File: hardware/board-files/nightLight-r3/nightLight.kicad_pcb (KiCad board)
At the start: 2 copper layers, 85 x 85 mm, 41 parts, among them IC1 PAM2401SCADJ, IC2 MCP73123T-22SI_MF, J1 USB_C_Receptacle_PowerOnly_6P, J2 Conn_01x03, J3 Conn_01x03, J4 Conn_01x03, J5 Conn_01x03, J6 Conn_01x05_Pin, SW1 TILT, U2 ATtiny1614-SS

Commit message: finished shematic and added to PCB
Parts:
- removed BT1: Battery_Cell, myFootprintDesigns:14500 Holder
- removed C7: 0.1uF, Capacitor_SMD:C_0805_2012Metric
- removed IC2: MCP73123T-22SI_MF, MCP73123T-22SI_MF:SON50P300X300X100-11N-D
- removed J6: Conn_01x05_Pin, Connector_PinSocket_2.54mm:PinSocket_1x05_P2.54mm_Vertical_SMD_Pin1Left
- removed LED1: IN-S124ARUW, KiCad-SMTLED:INS124ARUW
- removed R12: 10k, Resistor_SMD:R_0805_2012Metric
- removed R13: 1M, Resistor_SMD:R_0805_2012Metric
- removed S1: PTS526_SM08_SMTR2_LFS, PTS526_SM08_SMTR2_LFS:SW_PTS526_SM08_SMTR2_LFS
- removed U2: ATtiny1614-SS, Package_SO:SOIC-14_3.9x8.7mm_P1.27mm
- added BT2: Battery_Cell, myFootprintDesigns:14500 Holder, F.Cu at (66.0, 93.4)
- added C3: 22uF, Capacitor_SMD:C_0805_2012Metric, F.Cu at (39.2, 120.9)
- added C8: 4.7uF, Capacitor_SMD:C_0805_2012Metric, F.Cu at (61.6, 108.1)
- added D3: BAT54C, BAT54C:SOT23-R, F.Cu at (40.0, 116.6)
- added IC3: MCP73123T-22SI_MF, MCP73123T-22SI_MF:SON50P300X300X100-11N-D, F.Cu at (62.0, 104.3)
- added J7: USB_C_Receptacle_PowerOnly_6P, myFootprintDesigns:USB-C_PWR, F.Cu at (41.0, 108.2)
- added LED2: IN-S124ARUW, KiCad-SMTLED:INS124ARUW, F.Cu at (56.6, 105.6)
- added Q1: NMOS, IRLML6402TRPBF:SOT95P237X112-3N, F.Cu at (35.4, 117.1)
- added Q2: PMOS, IRLML6344TRPBF:SOT95P240X112-3N, F.Cu at (34.7, 121.5)
- added R1: 750K, Resistor_SMD:R_0805_2012Metric, F.Cu at (39.1, 123.9)
- added R14: 5.1k, Resistor_SMD:R_0805_2012Metric, F.Cu at (51.7, 103.4)
- added R15: 1K, Resistor_SMD:R_0805_2012Metric, F.Cu at (51.7, 106.4)
- added R16: 5.1K, Resistor_SMD:R_0805_2012Metric, F.Cu at (51.7, 109.3)
- added U1: ATtiny1614-SS, Package_SO:SOIC-14_3.9x8.7mm_P1.27mm, F.Cu at (48.3, 120.0)
- C2: value 4.7uF -> 0.1uF
- C4: value 4.7uF -> 22uF
- C5: value 22uF -> 4.7uF
- C6: value 22uF -> 0.1uF
- J1: value USB_C_Receptacle_PowerOnly_6P -> Conn_01x03; footprint myFootprintDesigns:USB-C_PWR -> Connector_PinHeader_2.54mm:PinHeader_1x03_P2.54mm_Vertical_SMD_Pin1Left
- J4: footprint Connector_PinHeader_2.54mm:PinHeader_1x03_P2.54mm_Vertical_SMD_Pin1Left -> myFootprintDesigns:spares_1*3
- J5: value Conn_01x03 -> Conn_01x05_Pin; footprint myFootprintDesigns:spares_1*3 -> Connector_PinSocket_2.54mm:PinSocket_1x05_P2.54mm_Vertical_SMD_Pin1Left
- R10: value 0 -> 10k
- R11: value 10k -> 1M
- R2: value 5.1k -> 1M
- R4: value 5.1k -> 10K
- R5: value 5.1K -> 1M
- R6: value 1K -> 0
- R7: value 750K -> 100K
- R8: value 100K -> 5.1k
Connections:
- B1 pad 1: Return -> /MCU/RETURN
- C1 pad 1: VBATT -> Net-(IC1-VIN)
- C2 pad 1: Net-(IC2-VDD_1) -> Net-(Q1-G)
- C4 pad 1: VBATT -> +5V
- C5 pad 1: +5V -> /Charge Controller/Vbus
- IC1 pad 3: VBATT -> Net-(IC1-VIN)
- J2 pad 2: LED_DATA -> Net-(J2-Pin_2)
- J3 pad 2: Net-(J3-Pin_2) -> Net-(J2-Pin_2)
- J4 pad 1: +5V -> /MCU/PA_1
- J4 pad 2: Net-(J3-Pin_2) -> /MCU/PA_2
- J4 pad 3: GND -> /MCU/PA_3
- J5 pad 1: PA_1 -> GND
- J5 pad 2: PA_2 -> /MCU/TX
- J5 pad 3: PA_3 -> /MCU/RX
- L1 pad 1: VBATT -> Net-(IC1-VIN)
- R10 pad 1: Batt_M -> +5V
- R10 pad 2: GND -> /MCU/TILT_SW
- R11 pad 1: +5V -> /MCU/SEND
- R11 pad 2: RST_SW -> /MCU/RETURN
- R2 pad 1: Net-(J1-CC2) -> /Charge Controller/Vbatt
- R2 pad 2: GND -> Net-(Q1-D)
- R3 pad 1: VBATT -> Net-(IC1-FB)
- R3 pad 2: Net-(IC1-EN) -> +5V
- R4 pad 1: Net-(J1-CC1) -> Net-(Q1-G)
- R4 pad 2: GND -> Net-(D3-Pad3)
- R5 pad 1: Net-(IC2-PROG) -> Net-(Q1-G)
- R6 pad 1: Net-(LED1-K) -> /Charge Controller/Vbatt
- R6 pad 2: Net-(IC2-STAT) -> /MCU/BATT_M
- R7 pad 1: Net-(IC1-FB) -> GND
- R7 pad 2: +5V -> Net-(IC1-FB)
- R8 pad 1: GND -> Net-(J7-CC2)
- R8 pad 2: Net-(IC1-FB) -> GND
- R9 pad 1: VBATT -> /MCU/BATT_M
- R9 pad 2: Batt_M -> GND
- SW1 pad 1: Tilt_SW -> /MCU/TILT_SW
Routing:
- net (no net): track 0.00 -> 85.0 mm
- net Net-(Q1-G): track 0.00 -> 73.0 mm
- net /Charge Controller/Vbatt: track 0.00 -> 58.8 mm
- net Net-(IC2-VDD_1): track 58.4 -> 0.00 mm
- net Net-(LED1-K): track 50.8 -> 0.00 mm
- net /MCU/RETURN: track 0.00 -> 36.8 mm
- net VBATT: track 20.3 -> 0.00 mm
- net RX: track 19.8 -> 0.00 mm
- net Return: track 18.7 -> 0.00 mm
- net RST_SW: track 18.1 -> 0.00 mm
- net Batt_M: track 17.6 -> 0.00 mm, vias 2 -> 0
- net Net-(J1-CC1): track 14.6 -> 0.00 mm
- net TX: track 14.4 -> 0.00 mm
- net Tilt_SW: track 9.29 -> 0.00 mm
- net /MCU/TILT_SW: track 0.00 -> 9.29 mm
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- added copper zone on F.Cu, net Net-(IC1-VIN)
- added copper zone on F.Cu, net Net-(Q1-G)
- removed copper zone on F.Cu, net Net-(IC2-PROG)
- removed copper zone on F.Cu, net Net-(IC2-VDD_1)
- removed copper zone on F.Cu, net VBATT

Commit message: first layout revision
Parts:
- removed BT2: Battery_Cell, myFootprintDesigns:14500 Holder
- removed C8: 4.7uF, Capacitor_SMD:C_0805_2012Metric
- removed D3: BAT54C, BAT54C:SOT23-R
- removed IC3: MCP73123T-22SI_MF, MCP73123T-22SI_MF:SON50P300X300X100-11N-D
- removed J7: USB_C_Receptacle_PowerOnly_6P, myFootprintDesigns:USB-C_PWR
- removed LED2: IN-S124ARUW, KiCad-SMTLED:INS124ARUW
- removed R15: 1K, Resistor_SMD:R_0805_2012Metric
- removed R16: 5.1K, Resistor_SMD:R_0805_2012Metric
- removed U9: ~, myFootprintDesigns:fireflyTouchNB
- added BT1: Battery_Cell, myFootprintDesigns:14500 Holder, F.Cu at (150.0, 100.0)
- added C7: 0.1uF, Capacitor_SMD:C_0805_2012Metric, F.Cu at (151.9, 84.0)
- added D1: BAT54C, BAT54C:SOT23-R, F.Cu at (184.2, 89.5)
- added IC2: MCP73123T-22SI_MF, MCP73123T-22SI_MF:SON50P300X300X100-11N-D, F.Cu at (177.2, 110.5)
- added J6: Conn_01x03, Connector_PinHeader_2.54mm:PinHeader_1x03_P2.54mm_Vertical_SMD_Pin1Left, F.Cu at (167.0, 115.0)
- added LED1: IN-S124ARUW, KiCad-SMTLED:INS124ARUW, F.Cu at (139.0, 131.0)
- added R12: 1M, Resistor_SMD:R_0805_2012Metric, F.Cu at (162.5, 80.0)
- added R13: 10k, Resistor_SMD:R_0805_2012Metric, F.Cu at (126.0, 78.0)
- added U2: ~, myFootprintDesigns:fireflyTouchNB, B.Cu at (132.0, 122.5)
- C1: value 22uF -> 0.1uF
- C2, C6: value 0.1uF -> 22uF
- C4: value 22uF -> 4.7uF
- J1: value Conn_01x03 -> USB_C_Receptacle_PowerOnly_6P; footprint Connector_PinHeader_2.54mm:PinHeader_1x03_P2.54mm_Vertical_SMD_Pin1Left -> myFootprintDesigns:USB-C_PWR
- J2: value Conn_01x03 -> Conn_01x05_Pin; footprint Connector_PinHeader_2.54mm:PinHeader_1x03_P2.54mm_Vertical_SMD_Pin1Left -> Connector_PinSocket_2.54mm:PinSocket_1x05_P2.54mm_Vertical_SMD_Pin1Left
- J3: footprint Connector_PinHeader_2.54mm:PinHeader_1x03_P2.54mm_Vertical_SMD_Pin1Left -> myFootprintDesigns:spares_1*3
- J4: footprint myFootprintDesigns:spares_1*3 -> Connector_PinHeader_2.54mm:PinHeader_1x03_P2.54mm_Vertical_SMD_Pin1Left
- J5: value Conn_01x05_Pin -> Conn_01x03; footprint Connector_PinSocket_2.54mm:PinSocket_1x05_P2.54mm_Vertical_SMD_Pin1Left -> Connector_PinHeader_2.54mm:PinHeader_1x03_P2.54mm_Vertical_SMD_Pin1Left
- R1: value 750K -> 10K
- R10: value 10k -> 5.1k
- R14: value 5.1k -> 1M
- R3: value 750K -> 1M
- R4: value 10K -> 750K
- R5: value 1M -> 750K
- R6: value 0 -> 100K
- R7: value 100K -> 1K
- R8: value 5.1k -> 5.1K
- R9: value 0 -> 5.1k
- U1: value ATtiny1614-SS -> ~; footprint Package_SO:SOIC-14_3.9x8.7mm_P1.27mm -> myFootprintDesigns:fireflyTouchNB; moved to B.Cu
- U8: value ~ -> ATtiny1614-SS; footprint myFootprintDesigns:fireflyTouchNB -> Package_SO:SOIC-14_3.9x8.7mm_P1.27mm; moved to F.Cu
- moved Q1 151.3 mm to (185.2, 96.5), turned to 180 degrees
- moved R1 150.5 mm to (186.2, 92.2), turned to 90 degrees
- moved Q2 149.8 mm to (182.0, 94.5), turned to -90 degrees
- moved C3 145.0 mm to (178.9, 82.5), turned to 180 degrees
- moved U1 123.8 mm to (172.1, 123.5), turned to 75 degrees
- moved R14 110.8 mm to (160.0, 80.0), turned to 90 degrees
- moved U8 50.5 mm to (144.0, 81.5), turned to 180 degrees
- moved R9 45.3 mm to (157.5, 125.0)
- moved R10 45.0 mm to (161.0, 125.0), turned to -90 degrees
- moved J4 44.8 mm to (144.0, 73.0), turned to -90 degrees
- moved R4 43.1 mm to (178.9, 85.8), turned to 180 degrees
- moved J3 42.5 mm to (135.3, 86.7), turned to 0 degrees
- moved R2 36.4 mm to (184.2, 100.2), turned to 90 degrees
- moved R8 33.5 mm to (176.8, 113.7), turned to 0 degrees
- moved R5 30.7 mm to (168.6, 84.1), turned to -90 degrees
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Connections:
- C1 pad 1: Net-(IC1-VIN) -> Net-(Q1-G)
- C2 pad 1: Net-(Q1-G) -> +5V
- C3 pad 1: +5V -> Net-(IC1-VIN)
- C4 pad 1: +5V -> /Charge Controller/Vbus
- C5 pad 1: /Charge Controller/Vbus -> /Charge Controller/Vbatt
- J2 pad 1: +5V -> GND
- J2 pad 2: Net-(J2-Pin_2) -> /MCU/TX
- J2 pad 3: GND -> /MCU/RX
- J3 pad 1: +5V -> /MCU/PA_1
- J3 pad 2: Net-(J2-Pin_2) -> /MCU/PA_2
- J3 pad 3: GND -> /MCU/PA_3
- J4 pad 1: /MCU/PA_1 -> +5V
- J4 pad 2: /MCU/PA_2 -> /MCU/LED_DATA
- J4 pad 3: /MCU/PA_3 -> GND
- J5 pad 1: GND -> +5V
- J5 pad 2: /MCU/TX -> Net-(J5-Pin_2)
- J5 pad 3: /MCU/RX -> GND
- R1 pad 1: Net-(IC1-VIN) -> Net-(Q1-G)
- R1 pad 2: Net-(IC1-EN) -> Net-(D1-Pad3)
- R10 pad 1: +5V -> Net-(J1-CC1)
- R10 pad 2: /MCU/TILT_SW -> GND
- R14 pad 1: Net-(J7-CC1) -> /MCU/BATT_M
- R3 pad 1: Net-(IC1-FB) -> Net-(Q1-G)
- R3 pad 2: +5V -> GND
- R4 pad 1: Net-(Q1-G) -> Net-(IC1-VIN)
- R4 pad 2: Net-(D3-Pad3) -> Net-(IC1-EN)
- R5 pad 1: Net-(Q1-G) -> Net-(IC1-FB)
- R5 pad 2: GND -> +5V
- R6 pad 1: /Charge Controller/Vbatt -> GND
- R6 pad 2: /MCU/BATT_M -> Net-(IC1-FB)
- R7 pad 1: GND -> Net-(LED1-K)
- R7 pad 2: Net-(IC1-FB) -> Net-(IC2-STAT)
- R9 pad 1: /MCU/BATT_M -> Net-(J1-CC2)
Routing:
- net /Charge Controller/Vbus: track 0.00 -> 94.7 mm
- net (no net): track 85.0 -> 0.00 mm
- net Net-(Q1-G): track 73.0 -> 13.1 mm
- net Net-(LED1-K): track 0.00 -> 50.8 mm
- net /MCU/FET_CONTROL: track 0.00 -> 47.5 mm, vias 0 -> 2
- net Net-(J5-Pin_2): track 0.00 -> 38.4 mm
- net Net-(J3-Pin_2): track 38.4 -> 0.00 mm
- net /MCU/RX: track 0.00 -> 19.8 mm
- net /MCU/RETURN: track 36.8 -> 18.7 mm
- net /MCU/BATT_M: track 1.86 -> 17.6 mm, vias 0 -> 2
- net /Charge Controller/Vbatt: track 58.8 -> 44.0 mm
- net Net-(J1-CC1): track 0.00 -> 14.6 mm
- net Net-(Q1-D): track 0.00 -> 9.90 mm
- net /MCU/SEND: track 0.00 -> 9.00 mm
- net /MCU/PA_1: track 0.00 -> 8.38 mm
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- removed copper zone on F.Cu, net Net-(Q1-G)

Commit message: PCB rev 3.1 done
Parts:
- Q1: value NMOS -> AO3400A; footprint IRLML6402TRPBF:SOT95P237X112-3N -> Package_TO_SOT_SMD:SOT-23
- Q2: value PMOS -> AO3401A; footprint IRLML6344TRPBF:SOT95P240X112-3N -> Package_TO_SOT_SMD:SOT-23
- moved R2 5.08 mm to (181.4, 104.5), turned to 0 degrees
- moved Q1 3.36 mm to (182.8, 98.8), turned to -90 degrees
- moved BT1 3.00 mm to (147.0, 100.0)
- moved R1 2.55 mm to (183.8, 92.8)
- moved Q2 2.50 mm to (179.5, 94.5), turned to 180 degrees
- moved R3 2.30 mm to (185.0, 103.8)
- moved C1 1.90 mm to (185.8, 99.8), turned to 90 degrees
- moved D1 1.75 mm to (182.5, 89.5)
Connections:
- Q1 pad 1: Net-(Q1-D) -> Net-(Q1-G)
- Q1 pad 2: Net-(Q1-G) -> GND
- Q1 pad 3: GND -> Net-(Q1-D)
- Q2 pad 1: Net-(IC1-VIN) -> Net-(Q1-D)
- Q2 pad 2: Net-(Q1-D) -> Net-(IC1-VIN)
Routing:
- net /Charge Controller/Vbatt: track 44.0 -> 34.3 mm
- net Net-(IC1-VIN): track 6.25 -> 0.00 mm
- net Net-(Q1-G): track 13.1 -> 10.4 mm
- net Net-(IC2-PROG): track 0.00 -> 2.27 mm
- net /Charge Controller/Vbus: track 94.7 -> 96.5 mm
- net /MCU/FET_CONTROL: track 47.5 -> 46.1 mm
- net Net-(D1-Pad3): track 2.35 -> 1.65 mm
- net Net-(Q1-D): track 9.90 -> 10.4 mm
- added copper zone on F.Cu, net /Charge Controller/Vbatt
- added copper zone on F.Cu, net /Charge Controller/Vbus
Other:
- board text added: "Night Light R3 Cameron Gillingham March 11, 2025"
- board text removed: "Night Light R2 Cameron Gillingham March 11, 2025"

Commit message: rev3 done, errors eliminated
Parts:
- added R15: 0, Resistor_SMD:R_0805_2012Metric, F.Cu at (152.3, 71.5)
- added R16: 0, Resistor_SMD:R_0805_2012Metric, F.Cu at (149.6, 71.5)
- J4, J5, J6: footprint Connector_PinHeader_2.54mm:PinHeader_1x03_P2.54mm_Vertical_SMD_Pin1Left -> myFootprintDesigns:fairy_conn
- moved SW1 1.80 mm to (129.2, 76.0)
- moved J5 1.50 mm to (128.0, 116.4), turned to 0 degrees
- moved J4 1.50 mm to (144.0, 71.5), turned to 180 degrees
- moved J6 0.45 mm to (166.6, 114.8), turned to 180 degrees
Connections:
- J2 pad 2: /MCU/TX -> Net-(J2-Pin_2)
- J2 pad 3: /MCU/RX -> Net-(J2-Pin_3)
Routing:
- net Net-(J2-Pin_3): track 0.00 -> 27.9 mm
- net Net-(J2-Pin_2): track 0.00 -> 17.7 mm
- net /MCU/RX: track 19.8 -> 11.3 mm
- net /MCU/TX: track 14.4 -> 8.26 mm
- net /MCU/LED_DATA: track 4.81 -> 8.99 mm
- net +5V: track 141.1 -> 144.5 mm
- net Net-(J5-Pin_2): track 38.4 -> 40.8 mm
- net /MCU/PA_1: track 8.38 -> 9.49 mm
- net /MCU/PA_3: track 4.33 -> 5.26 mm
- net /MCU/PA_2: track 6.35 -> 7.29 mm
- net GND: vias 163 -> 169

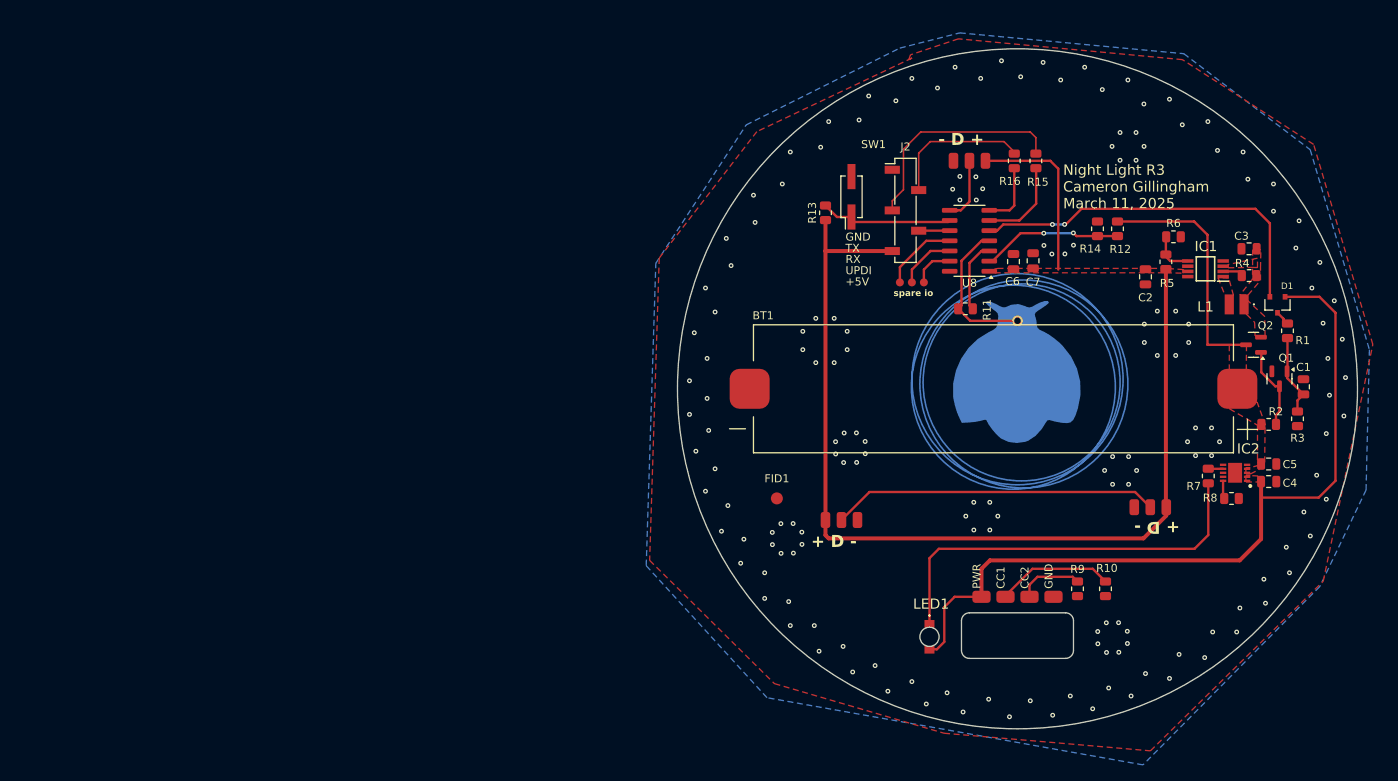
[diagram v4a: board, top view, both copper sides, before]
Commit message: PCB R3 Finished and ordered
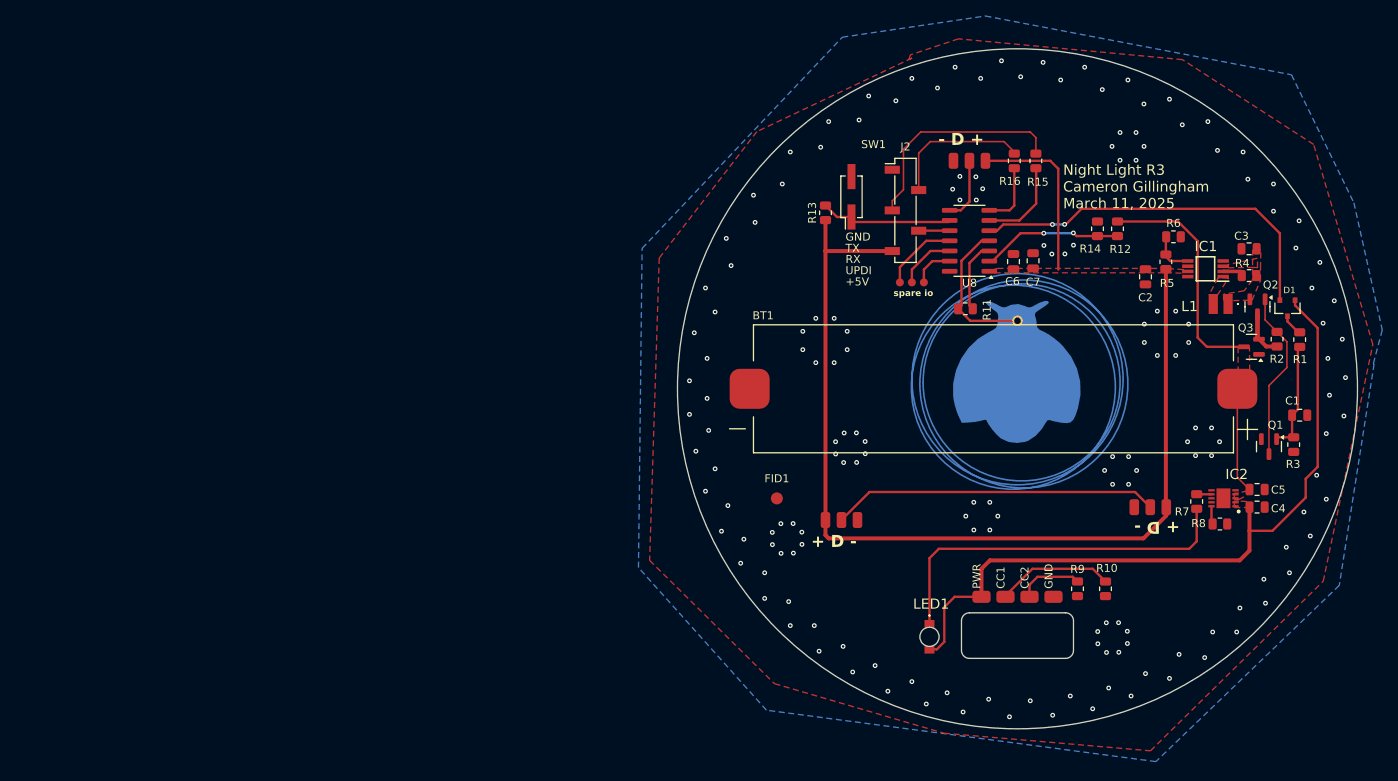
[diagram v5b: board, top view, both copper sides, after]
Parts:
- added Q3: AO3401A, Package_TO_SOT_SMD:SOT-23, F.Cu at (179.2, 94.8)
- moved R2 10.7 mm to (182.4, 93.8), turned to 90 degrees
- moved Q1 8.58 mm to (181.4, 107.2)
- moved Q2 4.78 mm to (180.0, 89.8), turned to -90 degrees
- moved C1 3.58 mm to (185.3, 103.3), turned to 0 degrees
- moved C4 3.50 mm to (179.9, 114.8)
- moved C5 3.50 mm to (179.9, 112.6)
- moved IC2 3.50 mm to (175.8, 113.7)
- moved R7 3.50 mm to (172.4, 114.1)
- moved R8 3.50 mm to (175.3, 116.9)
- moved R3 3.26 mm to (184.5, 107.0)
- moved L1 2.00 mm to (175.4, 89.4)
- moved R1 1.88 mm to (185.3, 93.8)
- moved D1 1.32 mm to (183.8, 89.9)
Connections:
- Q2 pad 3: /Charge Controller/Vbatt -> Net-(Q2-D)
- R2 pad 1: /Charge Controller/Vbatt -> Net-(Q2-D)
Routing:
- net Net-(Q1-D): track 10.4 -> 21.4 mm
- net /Charge Controller/Vbatt: track 34.3 -> 43.9 mm
- net /Charge Controller/Vbus: track 96.7 -> 90.2 mm
- net Net-(Q2-D): track 0.00 -> 5.83 mm
- net Net-(LED1-K): track 50.8 -> 46.6 mm
- net Net-(Q1-G): track 10.4 -> 14.0 mm
- net /MCU/FET_CONTROL: track 46.1 -> 47.1 mm
- net Net-(D1-Pad3): track 1.65 -> 2.50 mm
